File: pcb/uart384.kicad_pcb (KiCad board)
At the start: 2 copper layers, 56.6 x 23.5 mm, 32 parts, among them IC1 ICE40LP384-SG32, J1 USB_A, J2 TC2050, J3 Conn_02x06_Odd_Even, SW1 SW_Push, U1 CP2102-QFN28, U2 AT25DF256-XMHN-T, U3 MIC5365-1.2YC5, Y1 XO32

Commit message: PCBv1 Errata: Mismatch between SPI flash footprint and selected part#.
Part now must be SOIC-8 150mil / SOP-8 150mil.
Updated part#s in schematic / PCB.
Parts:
- U2: value AT25DF256-XMHN-T -> AT25DF256-SSHN
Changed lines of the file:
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@@
 	(title_block
 		(title "UART384")
-		(date "2025-08-26")
-		(rev "v1.0")
+		(rev "v1.1~dev")
 		(comment 1 "a USB/UART enabled dev-board for the ice40LP384")
 		(comment 2 "https://github.com/dpiegdon/uart384")
@@
 			)
 		)
-		(property "Value" "AT25DF256-XMHN-T"
+		(property "Value" "AT25DF256-SSHN"
 			(at 0 3.4 90)
 			(layer "F.Fab")
@@
 			)
 		)
-		(property "Description" "8-Mbit, 2.5V Minimum SPI Serial Flash Memory with Dual-I/O and Quad-I/O Support, SOIC-8"
+		(property "Description" "Any 3.3V SPI flash with >= 128KBit, SOIC-8 150mil or SOP-8 150mil"
 			(at 0 0 90)
 			(layer "F.Fab")

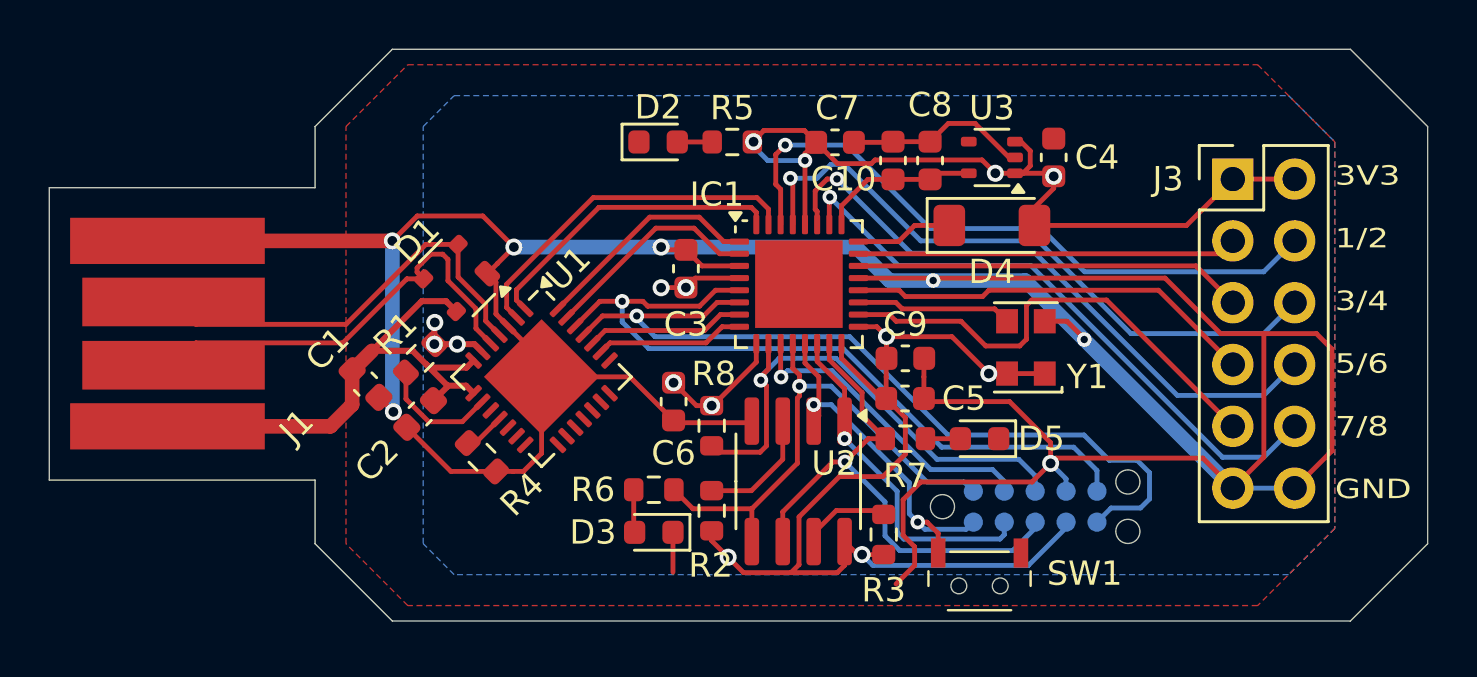
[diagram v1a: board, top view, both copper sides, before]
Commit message: PCBv1 Errata: SPI SS pullup missing
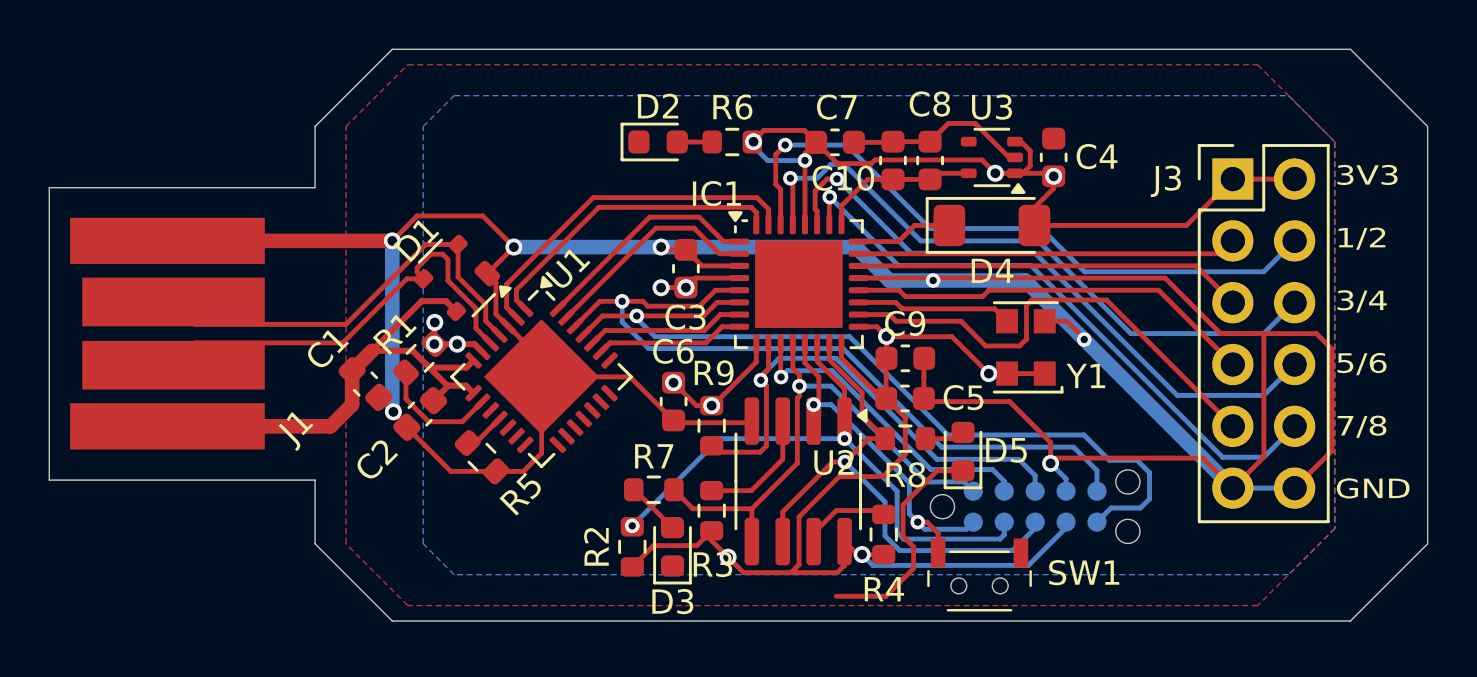
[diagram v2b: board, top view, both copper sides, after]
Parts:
- added R2: 10K, Resistor_SMD:R_0603_1608Metric, F.Cu at (100.2, 85.0)
- moved D3 0.97 mm to (101.9, 85.0), turned to 90 degrees
- moved D5 0.86 mm to (113.8, 81.1), turned to 90 degrees
- renumbered R2 to R3, R3 to R4, R4 to R5, R5 to R6, R6 to R7, R7 to R8, R8 to R9
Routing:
- net /SS: track 13.5 -> 23.7 mm, vias 1 -> 2
- net +3V3: track 90.7 -> 94.6 mm
- net GND: track 162.6 -> 159.7 mm

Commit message: name LEDs with used colors. use LEDs for more things.
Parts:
- D2: value LED -> LED_ORANGE
- D3: value LED -> LED1_RED
- D5: value LED -> LED2_GREEN
- R8: value 1k -> 680
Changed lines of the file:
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@@
 			)
 		)
-		(property "Value" "1k"
+		(property "Value" "680"
 			(at 0 1.43 0)
 			(layer "F.Fab")
@@
 			)
 		)
-		(property "Value" "LED"
+		(property "Value" "LED_ORANGE"
 			(at 0 1.43 0)
 			(layer "F.Fab")
@@
 			)
 		)
-		(property "Value" "LED"
+		(property "Value" "LED2_GREEN"
 			(at 0 1.43 90)
 			(layer "F.Fab")
@@
 			)
 		)
-		(property "Value" "LED"
+		(property "Value" "LED1_RED"
 			(at 0 1.43 90)
 			(layer "F.Fab")

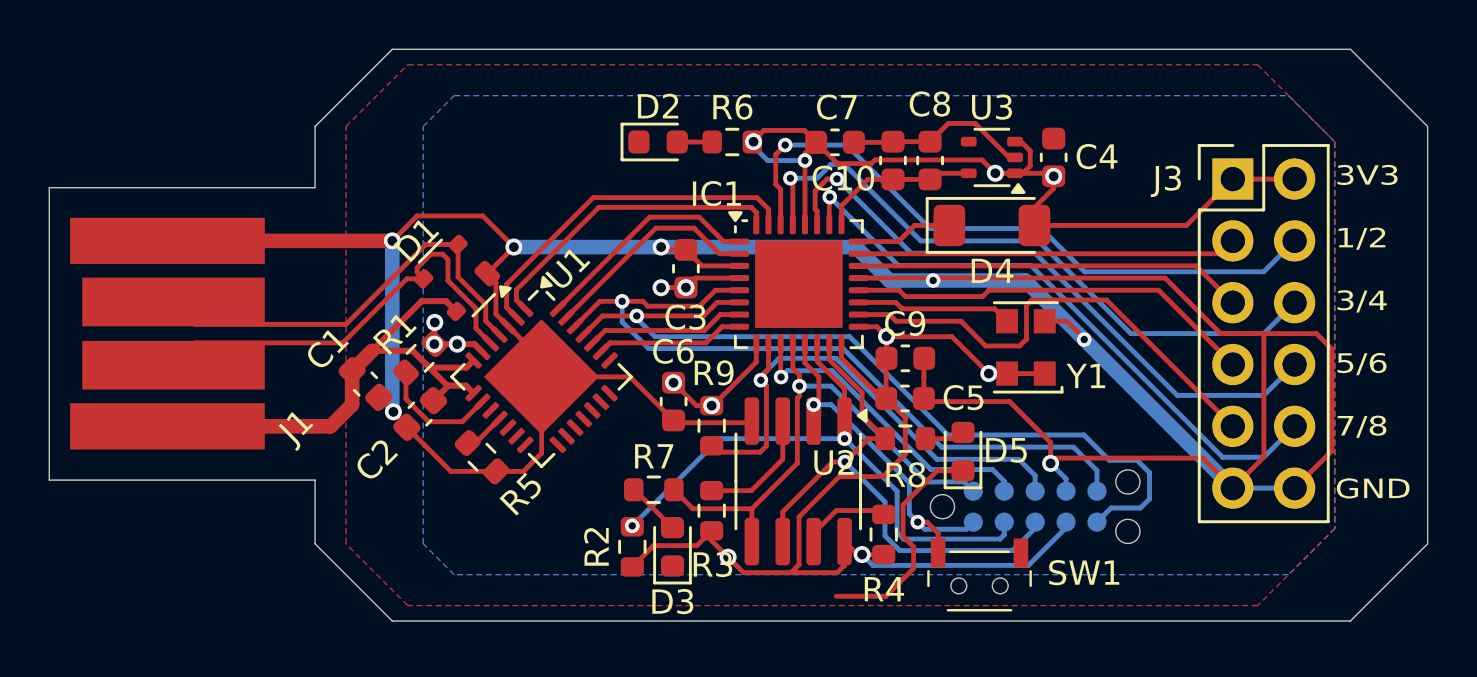
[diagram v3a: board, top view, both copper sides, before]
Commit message: PCB: add 5V to pinheader, move switch, LED, some resistors, improve routing
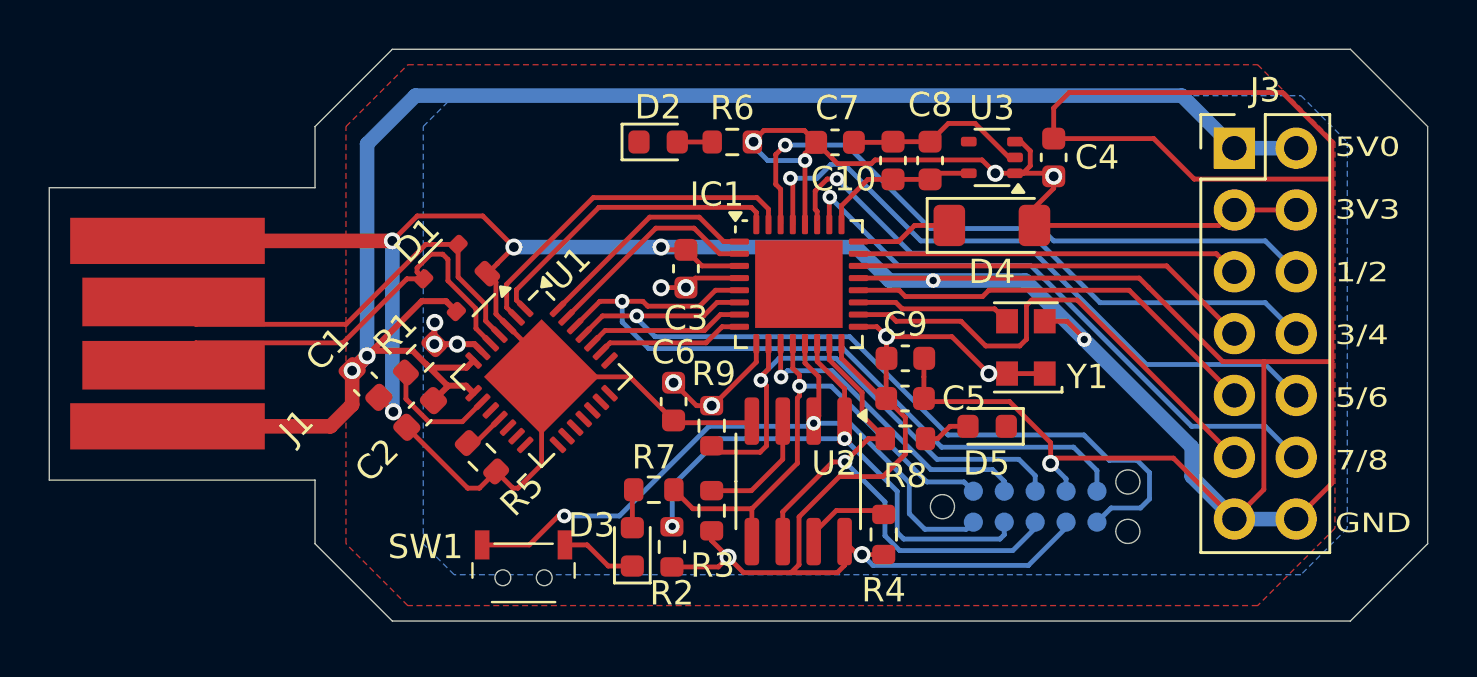
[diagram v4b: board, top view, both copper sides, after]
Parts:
- J3: value Conn_02x06_Odd_Even -> Conn_02x07_Odd_Even; footprint Connector_PinHeader_2.54mm:PinHeader_2x06_P2.54mm_Vertical -> Connector_PinHeader_2.54mm:PinHeader_2x07_P2.54mm_Vertical
- moved SW1 18.7 mm to (95.7, 86.2)
- moved D3 1.65 mm to (100.2, 85.0)
- moved R2 1.63 mm to (101.8, 85.0)
- moved D5 1.44 mm to (114.8, 80.0), turned to 180 degrees
- moved J3 1.27 mm to (124.9, 68.6)
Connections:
- J3 pad 1: +3V3 -> VBUS
- J3 pad 10: /GPIO8 -> /GPIO6
- J3 pad 11: GND -> /GPIO7
- J3 pad 12: GND -> /GPIO8
- J3 pad 2: +3V3 -> VBUS
- J3 pad 3: /GPIO1 -> +3V3
- J3 pad 4: /GPIO2 -> +3V3
- J3 pad 5: /GPIO3 -> /GPIO1
- J3 pad 6: /GPIO4 -> /GPIO2
- J3 pad 7: /GPIO5 -> /GPIO3
- J3 pad 8: /GPIO6 -> /GPIO4
- J3 pad 9: /GPIO7 -> /GPIO5
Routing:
- net VBUS: track 22.9 -> 72.6 mm, vias 0 -> 2
- net GND: track 159.7 -> 192.7 mm
- net /SDI: track 14.9 -> 28.4 mm
- net +3V3: track 94.6 -> 92.7 mm
- net /SS: track 23.7 -> 23.1 mm
- net Net-(D3-A): track 2.24 -> 1.62 mm
- net /GPIO7: track 19.7 -> 20.3 mm
- net /GPIO3: track 16.0 -> 16.6 mm
- net /GPIO5: track 16.9 -> 17.4 mm
- net Net-(D5-A): track 1.44 -> 1.96 mm
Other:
- board text added: "5V0 3V3 1/2 3/4 5/6 7/8 GND"
- board text added: "UART384 v1.1 by dpiegdon"
- board text removed: "3V3 1/2 3/4 5/6 7/8 GND"
- board text removed: "UART384 v1.0"
- board text removed: "by dpiegdon"

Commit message: PCB: add additional header for upstream TC2050, re-route PCB.
Adding J4 for the "other" side of a TC2050 cable allows programming a
UART384 with another UART384, once a gateware is written that also can
control CDONE and CRESET lines. This enables full bootstrapping of a
UART384 with a UART384 :-D
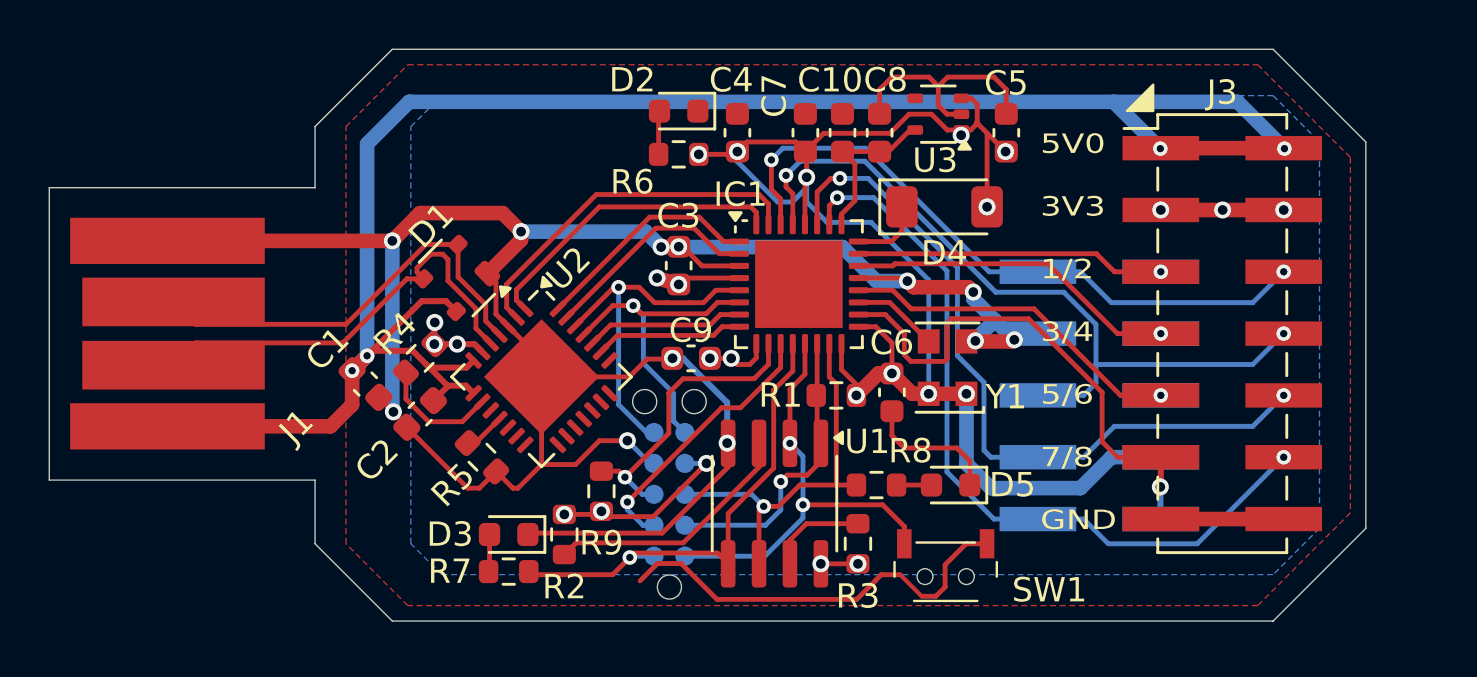
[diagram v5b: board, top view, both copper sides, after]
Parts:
- added J4: TC2050_ext, Connector_PinHeader_2.54mm:PinHeader_2x05_P2.54mm_Vertical_SMD, B.Cu at (119.4, 78.7)
- J3: footprint Connector_PinHeader_2.54mm:PinHeader_2x07_P2.54mm_Vertical -> Connector_PinHeader_2.54mm:PinHeader_2x07_P2.54mm_Vertical_SMD
- moved SW1 17.3 mm to (113.1, 86.2)
- moved J2 15.0 mm to (101.7, 82.8), turned to 90 degrees
- moved C4 13.0 mm to (104.5, 67.9)
- moved C5 11.7 mm to (115.6, 67.9), turned to 90 degrees
- moved R1 9.19 mm to (108.6, 78.7), turned to 180 degrees
- moved C6 8.98 mm to (110.9, 78.6)
- moved C9 8.81 mm to (102.6, 77.2), turned to 180 degrees
- moved J3 7.64 mm to (124.4, 76.2)
- moved R7 6.85 mm to (95.1, 86.0)
- moved R2 6.13 mm to (97.4, 84.5), turned to -90 degrees
- moved R9 5.27 mm to (98.9, 82.7), turned to 90 degrees
- moved D3 5.11 mm to (95.1, 84.5), turned to 180 degrees
- moved Y1 3.32 mm to (113.2, 77.6)
- moved D5 2.84 mm to (113.3, 82.4)
- moved U3 2.83 mm to (112.8, 67.2)
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- renumbered R2 to R1, R3 to R2, R4 to R3, R1 to R4, U2 to U1, U1 to U2
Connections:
- net /CLK32M renamed /CLK
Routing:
- net GND: track 192.7 -> 138.0 mm, vias 7 -> 12
- net /UART_RXD: track 34.4 -> 13.3 mm
- net /UART_TXD: track 31.3 -> 14.6 mm
- net /SS: track 23.1 -> 12.3 mm, vias 2 -> 1
- net /SDI: track 28.4 -> 18.4 mm
- net /CRESET_B: track 21.3 -> 12.2 mm
- net +3V3: track 92.7 -> 85.1 mm, vias 15 -> 25
- net VBUS: track 72.6 -> 79.8 mm, vias 2 -> 4
- net /GPIO8: track 24.7 -> 31.8 mm, vias 1 -> 2
- net /GPIO4: track 25.8 -> 32.3 mm, vias 1 -> 2
- net /SCK: track 22.3 -> 16.0 mm
- net Net-(U1-~{WP}/IO2): track 5.02 -> 10.5 mm
- net /GPIO6: track 25.1 -> 30.3 mm, vias 1 -> 2
- net /GPIO5: track 17.4 -> 14.2 mm, vias 0 -> 1
- net /GPIO1: track 15.8 -> 12.7 mm, vias 0 -> 1
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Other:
- board size 56.6 x 23.5 mm -> 54.1 x 23.5 mm

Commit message: PCB: add LP384 GND center pad from upstream symbol, improve schematic and routing
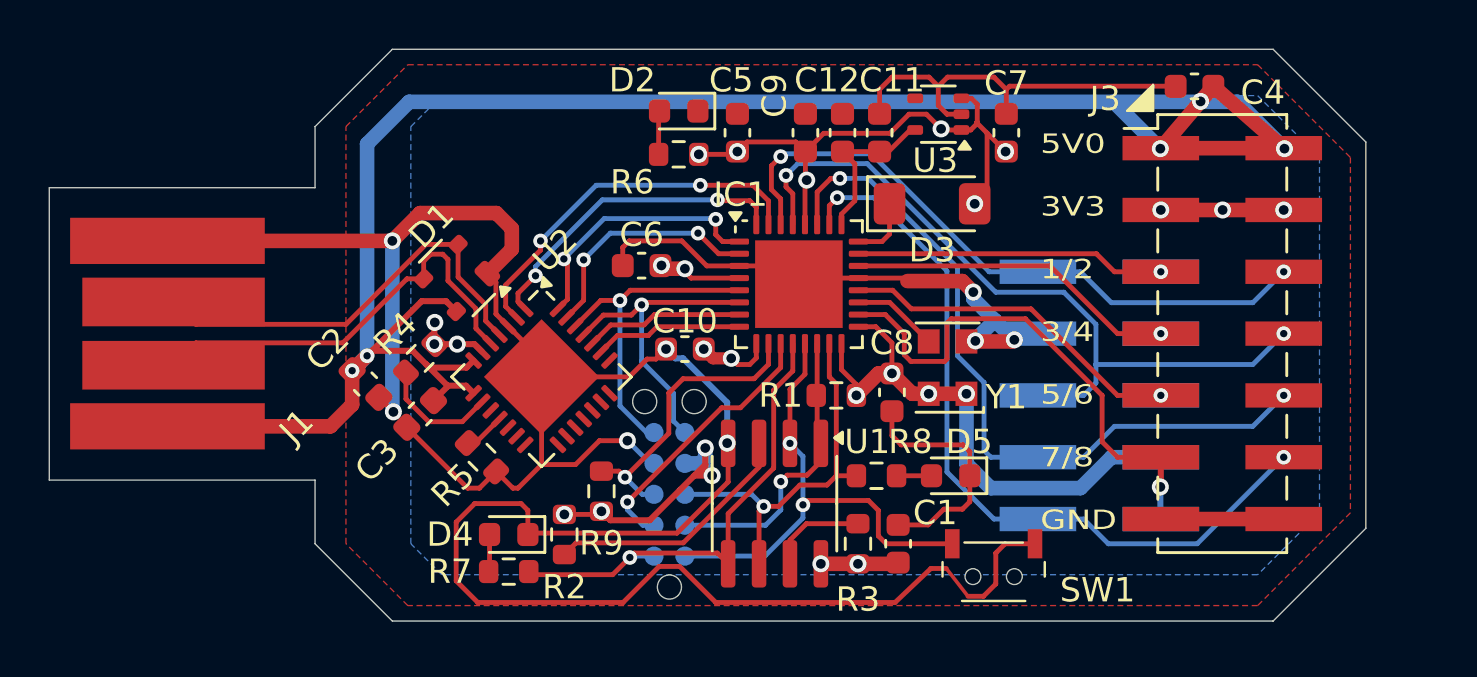
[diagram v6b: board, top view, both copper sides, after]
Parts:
- added C1: 100n, Capacitor_SMD:C_0603_1608Metric, F.Cu at (111.1, 84.8)
- added C4: 4u7, Capacitor_SMD:C_0603_1608Metric, F.Cu at (123.3, 66.0)
- R6, R7: value 1k -> 680
- moved SW1 1.97 mm to (115.1, 86.2)
- moved C6 1.52 mm to (100.6, 73.4), turned to 180 degrees
- moved D3 0.52 mm to (112.5, 70.9)
- moved C10 0.46 mm to (102.4, 76.8)
- moved D5 0.38 mm to (113.3, 82.0)
- moved R8 0.38 mm to (110.2, 82.0)
- renumbered C9 to C10, C8 to C11, C10 to C12, C1 to C2, C2 to C3, C4 to C5, C3 to C6, C5 to C7, C6 to C8, C7 to C9, D4 to D3, D3 to D4
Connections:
- IC1 pad 33: unconnected-(IC1-center_pad-Pad33) -> GND
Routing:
- net GND: track 138.0 -> 158.3 mm, vias 12 -> 8
- net +3V3: track 85.1 -> 73.8 mm, vias 25 -> 26
- net VBUS: track 79.8 -> 87.0 mm, vias 4 -> 5
- net /SDI: track 18.4 -> 20.6 mm
- net /UART_DTR: track 9.43 -> 10.9 mm, vias 0 -> 2
- net /UART_TXD: track 14.6 -> 13.5 mm
- net /UART_DSR: track 9.06 -> 9.86 mm, vias 0 -> 2
- net /UART_RI: track 14.8 -> 15.5 mm, vias 0 -> 2
- net /UART_DCD: track 12.8 -> 13.2 mm, vias 0 -> 2
